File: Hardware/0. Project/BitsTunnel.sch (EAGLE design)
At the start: 32 parts, among them IC1 RASPBERRY_PI_ZERO_W_(V1.3), IC3 DS3231/SO, IC5 LM1117-5V, IC6 LM1117-3.3V, IC7 LM317, K1 5V, T3 BC848

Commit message: New power supply approach
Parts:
- removed C13: 220uF x 16V, rcl:CPOL-EUC
- removed C15, C16: 10uF x 16V, rcl:CPOL-EUC
- removed C17: 2200uF x 35V, rcl:CPOL-EUC
- removed C18: 10uF x 25V, rcl:CPOL-EUB
- removed C19: 100nF, rcl:C-EUC0805
- removed C20: 1uF x 25V, rcl:CPOL-EUB
- removed D5, D6, D7: SM4007, diode:CGRM4007-G
- removed G3: 12V/1.3 mAh, battery:AB9V
- removed IC5: LM1117-5V, burr-brown:REG1117
- removed IC6: LM1117-3.3V, burr-brown:REG1117
- removed IC7: LM317, v-reg:LM317TS
- removed K1: 5V, relay:G5LE
- removed LED3: Green, led:LEDCHIP-LED0805
- removed R10: 10M, rcl:R-EU_M0805
- removed R23, R27: 4.7M, rcl:R-EU_M0805
- removed R30: 2k2, rcl:R-EU_R0805
- removed R31: 10R/3W, rcl:R-EU_0617/17
- removed R32: 470R, rcl:R-EU_M0805
- removed R33: 10k, rcl:R-TRIMMT93YA
- removed R34: 470R, rcl:R-EU_R0805
- removed T3: BC848, transistor:BC848
- removed X3: (no value), con-ptr500:AK500/2-H
- added BT1: 3.7V x 850mAh, Battery-Cable:BATTERY-3PIN
- added C1, C2: 22uF x 16V, rcl:C-EUC0805
- added C3, C4: 100nF, rcl:C-EUC0603
- added C5: 10UF, rcl:C-EUC0603
- added D1, D2, D3: SS16, diode:SUPPRESSOR-SMBJ
- added IC2: TP4056, TP4056:TP4056
- added IC4: DW01A-G, DW01A-G:DW01A-G
- added L1: 22 uH, Inductor:INDUCTOR
- added LED1, LED2: (no value), led:LEDCHIPLED_0805
- added Q1: AO3407 (IRLML9301TRPBF), IRLML6402:IRLML6402TRPBF
- added R1: 110k (±1%), rcl:R-EU_R0603
- added R2: 15k (±1%), rcl:R-EU_R0603
- added R3, R5, R7: 1k, rcl:R-EU_R0603
- added R4: 100R, rcl:R-EU_R0603
- added R8, R9: 100k, rcl:R-EU_R0603
- added U1: MT3608, MT3608:MT3608
- added U2: FS8205A, FS8205A:FS8205A
- R6: value 10M -> 1k; device rcl:R-EU_M0805 -> rcl:R-EU_R0603
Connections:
- removed net 13.8V: C13.+, D6.C, IC5.VIN, K12.O
- removed net 14.2V: C20.+, D5.A, D6.A, IC7.OUT, R32.2
- removed net BAT_ENABLE: R30.2, R34.2
- removed net BAT_SHUNT_INPUT: R23.2, R6.1
- removed net BAT_SHUNT_OUTPUT: R10.1, R27.2
- removed net N$23: G3.+, K12.P, R10.2, R31.1
- removed net N$24: R30.1, T3.B
- removed net N$27: D7.A, K11.2, T3.C
- removed net N$34: D5.C, R31.2, R6.2
- removed net N$37: C17.+, C19.1, IC7.IN, X3-1.KL
- removed net N$40: C18.+, IC7.ADJ, R32.1, R33.E
- removed net N$41: LED3.A, R34.1
- new net BAT_CHARGING: IC2.!CHRG, LED1.C
- new net BAT_STANDBY: IC2.!STDBY, LED2.C
- new net N$1: R1.1, R2.2, U1.FB
- new net N$10: BT1.-, C3.2, IC4.GND, U2.S1_1
- new net N$11: LED1.A, R6.1
- new net N$12: C5.1, Q1.S
- new net N$13: C1.1, L1.1, Q1.D, U1.EN, U1.IN
- new net N$14: LED2.A, R7.1
- new net N$15: Q1.G, R8.1, R9.2
- new net N$2: C2.1, D1.C, D2.A, R1.2
- new net N$3: D1.A, L1.2, U1.SW
- new net N$4: IC4.OD, U2.G1
- new net N$5: IC4.OC, U2.G2
- new net N$6: IC2.PROG2, R5.2
- new net N$7: IC4.CS, R3.2
- new net N$8: C3.1, IC4.VCC, R4.2
- new net POWER_SUPPLY_CONNECTED: C4.1, D3.A, IC2.CE, IC2.VCC4, R6.2, R7.2, R9.1
- net +5V: now also BT1.+, D2.C, D3.C, IC2.BAT, R4.1; no longer C15.+, D7.C, IC5.VOUT, IC6.VIN, K11.1
- net 3.3V: no longer C16.+, IC6.VOUT
- net GND: now also C1.2, C2.2, C4.2, C5.2, IC2.GND_3, IC2.TEMP1, R2.1, R3.1, R5.1, R8.2, U1.GND, U2.S2_1; no longer C13.-, C15.-, C16.-, C17.-, C18.-, C19.2, C20.-, G3.-, IC5.GND, IC6.GND, LED3.C, R23.1, R27.1, R33.A, R33.S, T3.E, X3-2.KL
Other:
- note added: "(Over-Charge & Over-Discharge)"
- note added: "BATTERY CHARGER"
- note added: "BATTERY PROTECTION"
- note added: "BOOST CONVERTER (DC-DC STEP UP)"
- note added: "LI-PO BATTERY"
- note added: "if external power supply connected --> Boost Converter is OFF"
- note removed: "Lead Acid Battery (VRLA)"
- note removed: "POWER SUPPLY & BATTERY BACKUP (NO-BREAK)"
- note removed: "Rele Status"
- moved on the sheet: R6

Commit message: DC-DC Step-UP Enabler Circuit Added
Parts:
- added C6, C7: 100nF, rcl:C-EUC0805
- added JP1: ICSP, pinhead:PINHD-2X3
- added R10: 20k, ptc-ntc:NTC640
- added R11: 50k, resistor:R-TRIMM64P
- added R12: 10k, rcl:R-EU_M0805
- added U3: ATMEGA328P-AU, Atmel_By_element14_Batch_1-00:ATMEGA328P-AU
- R8: value 100k -> 1M
- R9: value 100k -> 100R
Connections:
- new net +4.1V: IC1.+3.3V_1
- new net MISO_ICSP: JP1.1, U3.PD6
- new net MOSI_ICSP: JP1.4, U3.PD5
- new net N$16: IC2.TEMP1, R10.1, R11.E
- new net N$17: C6.2, U3.AREF
- new net RESET_UC: JP1.5, R12.1, U3.PC6
- new net SCK_ICSP: JP1.3, U3.PD7
- net +5V: now also R10.2
- net 3.3V: now also C7.2, JP1.2, R12.2, U3.AVCC, U3.VCC, U3.VCC_2
- net GND: now also C6.1, C7.1, JP1.6, R11.A, R11.S, U3.GND, U3.GND_2, U3.GND_3; no longer IC2.TEMP1
- net N$15: no longer R8.1
- net POWER_SUPPLY_CONNECTED: now also R8.1
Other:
- note added: "(Broadcom BCM2835 ARM11, Single-Core CPU, Bluetooth 4.1 and Wi-Fi)"
- note added: "BOOST CONVERTER ENABLER"
- note added: "RASPBERY PI ZERO W"
- note removed: "SINGLE-CORE 1 GHz ARM11 PROCESSOR / WI-FI / BLUETOOTH"
- note removed: "if external power supply connected --> Boost Converter is OFF"
- moved on the sheet: BT1, C1, C2, C3, C4, C5, D1, D2, D3, G1, IC1, IC2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

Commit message: ADC to I2C MCU based added
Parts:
- removed R15, R16: 4k7, rcl:R-EU_R0805
- added C8: 100nF, rcl:C-EUC0805
- added J1: (no value), con-jack:JACK-PLUG0
- added LED3: IN-PI556FCH, LED RGB SMD:IN-PI556FCH
- added R13: 150R (5%), rcl:R-EU_R0603
- added R14, R17: 50R (5%), rcl:R-EU_R0603
- added R18, R20, R21, R22, R26, R27: 10k, rcl:R-EU_M0805
- added R19, R23, R24, R25: 6k8, rcl:R-EU_M0805
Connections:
- net MISO_ICSP renamed ICSP_MISO
- net MOSI_ICSP renamed ICSP_MOSI
- net SCK_ICSP renamed ICSP_SCK
- removed net +4.1V: IC1.+3.3V_1
- removed net POWER_SUPPLY_CONNECTED: C4.1, D3.A, IC2.CE, IC2.VCC4, R6.2, R7.2, R8.1, R9.1
- removed net RESET_UC: JP1.5, R12.1, U3.PC6
- removed net RTC_SCL: IC1.GPIO_3/[I2C]_SCL, IC3.SCL, R15.1
- removed net RTC_SDA: IC1.GPIO_2/[I2C]_SDA, IC3.SDA, R16.1
- new net ICSP_RESET: JP1.5, R26.2, U3.PC6
- new net LED_BLUE: R17.1, U3.PB3
- new net LED_GREEN: R14.1, U3.PB2
- new net LED_RED: R13.1, U3.PB1
- new net N$18: R22.2, R25.1, U3.PC3
- new net N$19: R21.2, R24.1, U3.PC2
- new net N$20: R20.2, R23.1, U3.PC1
- new net N$21: LED3.AG1, R14.2
- new net N$22: R18.2, R19.1, U3.PC0
- new net N$26: LED3.AB3, R17.2
- new net RASPBERRY_SCL: IC1.GPIO_3/[I2C]_SCL, IC3.SCL, R27.2, U3.PC5
- new net RASPBERRY_SDA: IC1.GPIO_2/[I2C]_SDA, IC3.SDA, R12.2, U3.PC4
- new net V_BAT: BT1.+, IC2.BAT, R20.1, R4.1
- new net V_DC-DC: C2.1, D1.C, D2.A, R1.2, R21.1
- new net V_POWER_SUPPLY: C4.1, D3.A, IC2.CE, IC2.VCC4, J1.3, R18.1, R6.2, R7.2, R8.1, R9.1
- net +5V: now also R22.1; no longer BT1.+, IC2.BAT, R4.1
- net 3.3V: now also C8.2, IC1.+3.3V_1, IC1.+3.3V_2, R12.1, R26.1, R27.1; no longer R12.2, R15.2, R16.2
- net GND: now also C8.1, J1.1, J1.2, LED3.KB4, LED3.KG6, LED3.KR5, R19.2, R23.2, R24.2, R25.2
- net N$2: now also LED3.AR2, R13.2; no longer C2.1, D1.C, D2.A, R1.2
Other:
- note added: "(Monitoring and Status of Power Supply & Battery)"
- note added: "ADC TO I2C"
- note added: "USER INTERFACE"
- moved on the sheet: C1, C2, C6, C7, D1, D2, G1, IC1, IC3, JP1, L1, Q1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

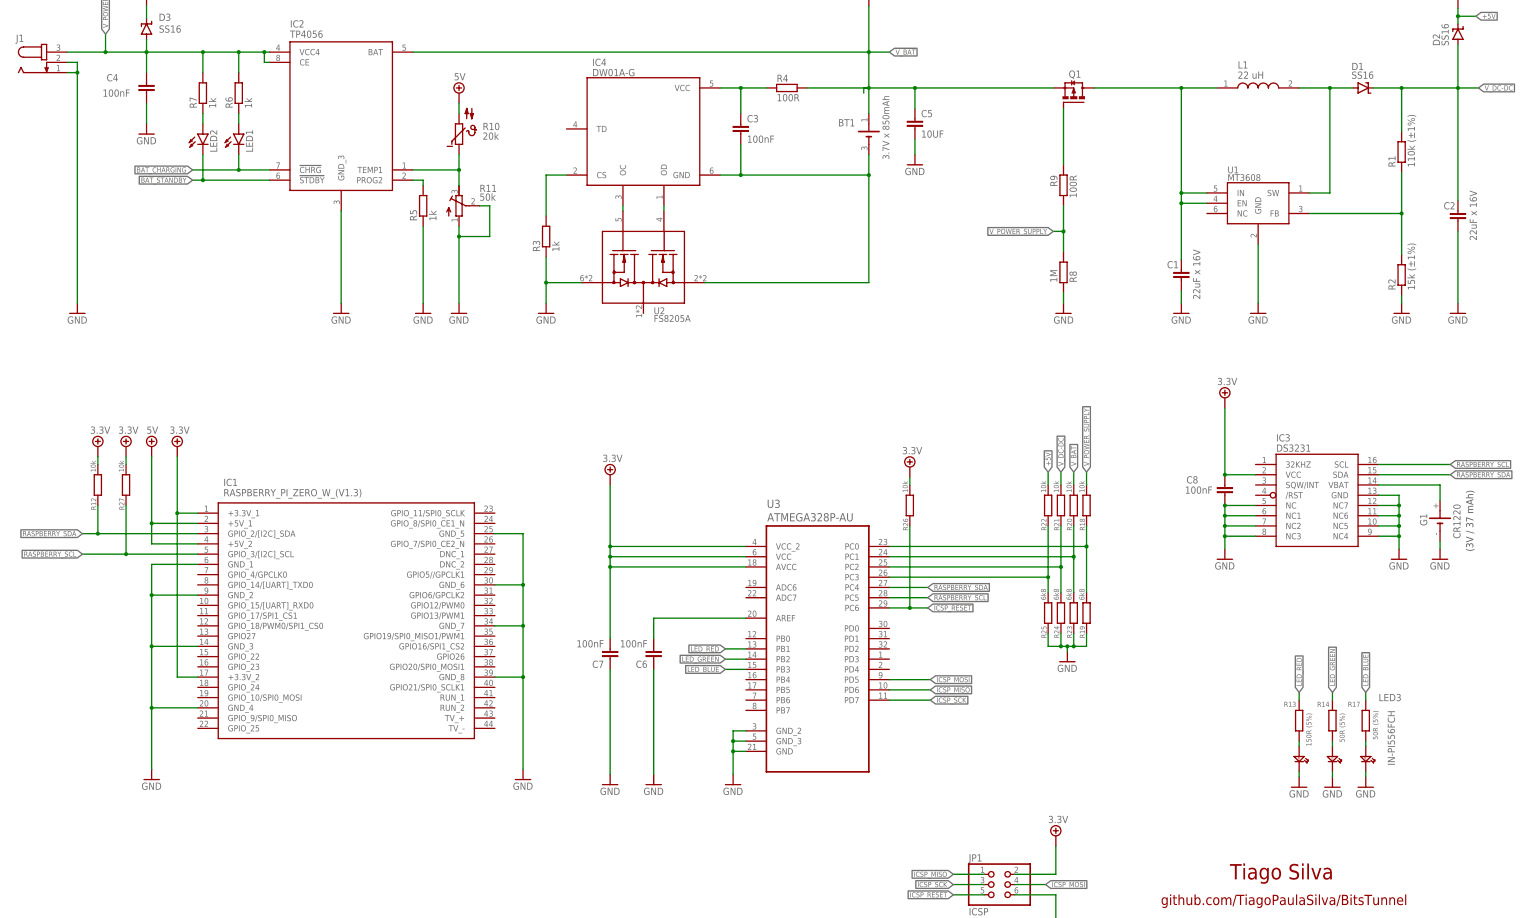
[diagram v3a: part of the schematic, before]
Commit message: OverChg. and OverDchg. pins monitoring added
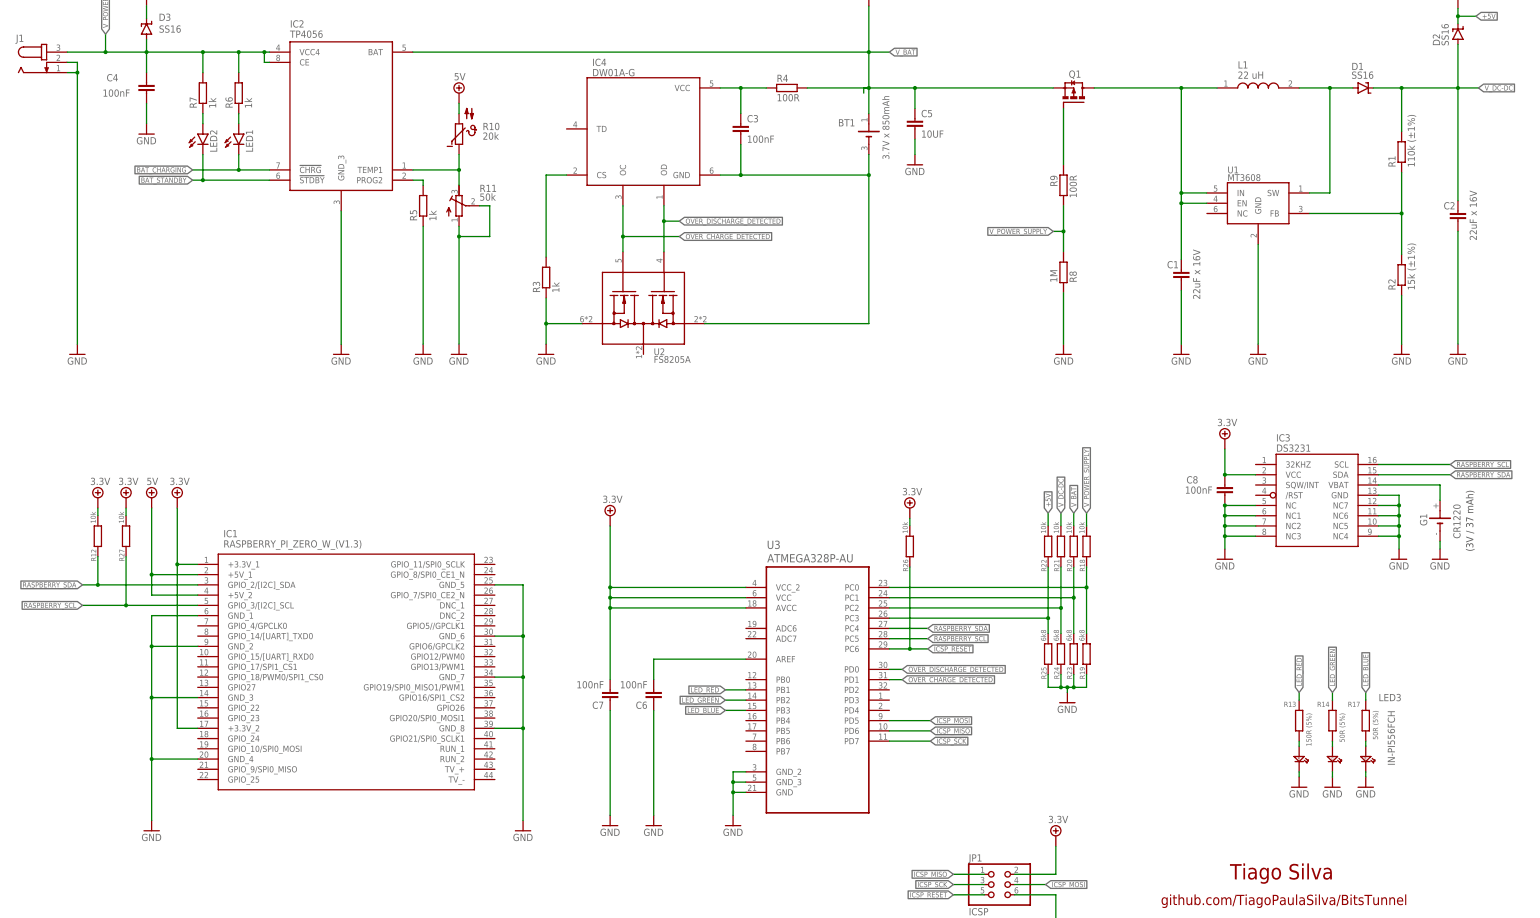
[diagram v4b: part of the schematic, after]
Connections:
- removed net N$4: IC4.OD, U2.G1
- removed net N$5: IC4.OC, U2.G2
- new net OVER_CHARGE_DETECTED: IC4.OC, U2.G2, U3.PD1
- new net OVER_DISCHARGE_DETECTED: IC4.OD, U2.G1, U3.PD0
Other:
- moved on the sheet: C6, C7, IC1, R12, R18, R19, R20, R21, R22, R23, R24, R25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

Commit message: ICSP MCU pins changed
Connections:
- removed net N$12: C5.1, Q1.S
- removed net OVER_CHARGE_DETECTED: IC4.OC, U2.G2, U3.PD1
- removed net OVER_DISCHARGE_DETECTED: IC4.OD, U2.G1, U3.PD0
- new net BAT_OVER_CHARGE_DETECTED: IC4.OC, U2.G2, U3.PD3
- new net BAT_OVER_DISCHARGE_DETECTED: IC4.OD, U2.G1, U3.PD2
- net BAT_CHARGING: now also U3.PD0
- net BAT_STANDBY: now also U3.PD1
- net ICSP_MISO: now also U3.PB4; no longer U3.PD6
- net ICSP_MOSI: now also U3.PB3; no longer U3.PD5
- net ICSP_SCK: now also U3.PB5; no longer U3.PD7
- net LED_BLUE: now also U3.PD6; no longer U3.PB3
- net LED_GREEN: now also U3.PD5; no longer U3.PB2
- net LED_RED: now also U3.PD4; no longer U3.PB1
- net V_BAT: now also C5.1, Q1.S
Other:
- note added: "(Power Supply & Battery Status Monitoring)"
- note removed: "(Monitoring and Status of Power Supply & Battery)"
- moved on the sheet: C1, C2, C3, C4, C8, D1, D2, D3, G1, IC2, IC3, IC4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

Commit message: Schematic minor improvements
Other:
- note added: "POWER SUPPLY & BATTERY STATUS MONITOR"
- note removed: "(Power Supply & Battery Status Monitoring)"
- note removed: "ADC TO I2C"
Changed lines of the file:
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@@
 <wire x1="145.415" y1="4.445" x2="283.21" y2="4.445" width="0.254" layer="152" style="longdash"/>
 <wire x1="283.21" y1="4.445" x2="283.21" y2="147.32" width="0.254" layer="152" style="longdash"/>
-<text x="204.47" y="141.605" size="2.54" layer="152" ratio="5">ADC TO I2C</text>
-<text x="188.595" y="137.795" size="2.032" layer="152">(Power Supply &amp; Battery Status Monitoring)</text>
+<text x="177.165" y="142.24" size="2.54" layer="152" ratio="5">POWER SUPPLY &amp; BATTERY STATUS MONITOR</text>
 </plain>
 <instances>
